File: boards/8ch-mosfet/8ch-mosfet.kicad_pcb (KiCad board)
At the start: 2 copper layers, 184.5 x 137 mm, 179 parts, among them J10 Screw_Terminal_01x02, J11 Screw_Terminal_01x02, J12 Screw_Terminal_01x02, J13 I2C, J14 N2K, J3 Screw_Terminal_01x08, J5 Screw_Terminal_01x02, J6 Screw_Terminal_01x02, J7 Screw_Terminal_01x02, J8 Screw_Terminal_01x02, J9 Screw_Terminal_01x02, M1 Fan_4pin, M2 Fan_4pin, Q1 2N7002, Q10 IRF4905, Q11 2N7002, Q12 IRF4905, Q13 2N7002, Q14 IRF4905, Q15 2N7002, Q16 IRF4905, Q2 IRF4905, Q3 2N7002, Q4 IRF4905, Q5 2N7002, Q6 IRF4905, Q7 2N7002, Q8 IRF4905, Q9 2N7002, U1 ESP32-DEVKITC, U10 ACS725xLCTR-20AU, U11 ACS725xLCTR-20AU, U12 ACS725xLCTR-20AU, U13 MCP1502-33, U15 MCP3425A0T-ECH, U2 MCP3208, U4 XL1509-5.0, U5 ACS725xLCTR-20AU, U6 ACS725xLCTR-20AU, U7 ACS725xLCTR-20AU, U8 ACS725xLCTR-20AU, U9 ACS725xLCTR-20AU

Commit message: updated BOM
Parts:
- F10: value mSMD100 -> mSMD110
- R10, R14, R18, R2, R22, R26, R30, R6: value 220 -> 220R

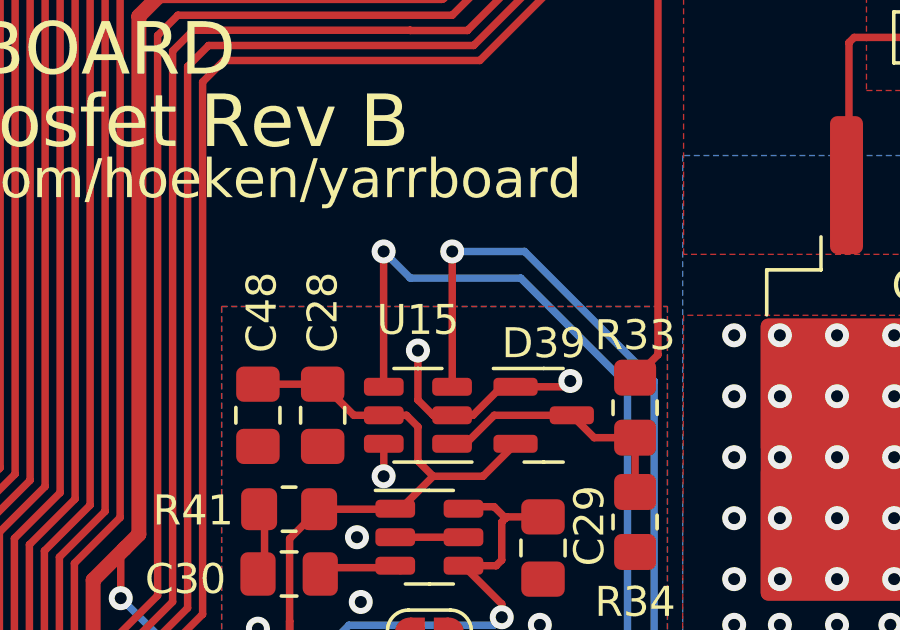
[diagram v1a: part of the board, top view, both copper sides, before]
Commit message: damnit, messed up the sda/scl lines on the board
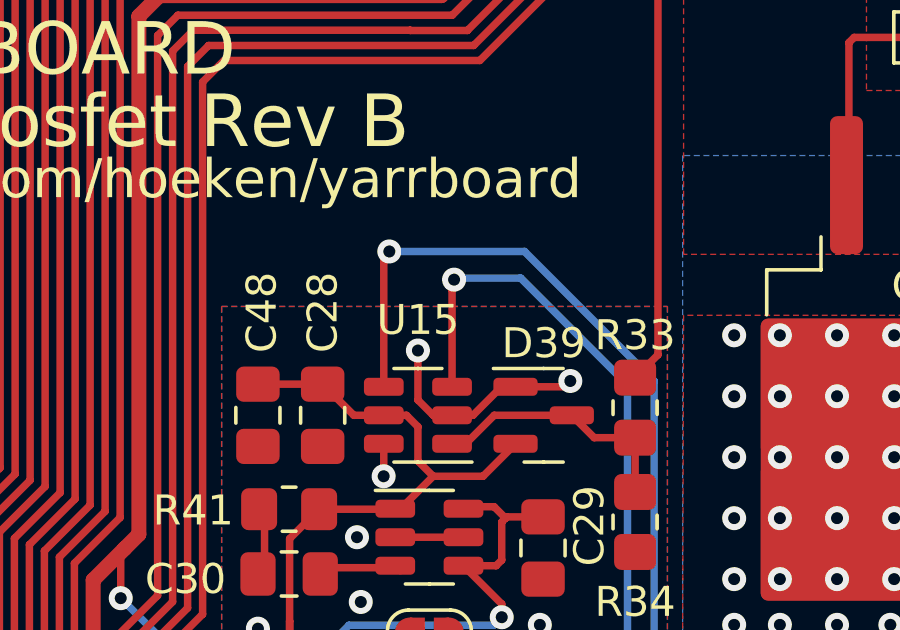
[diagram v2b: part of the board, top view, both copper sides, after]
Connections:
- U15 pad 3: SDA -> SCL
- U15 pad 4: SCL -> SDA
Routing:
- net SCL: track 85.2 -> 81.6 mm
- net SDA: track 88.8 -> 91.1 mm

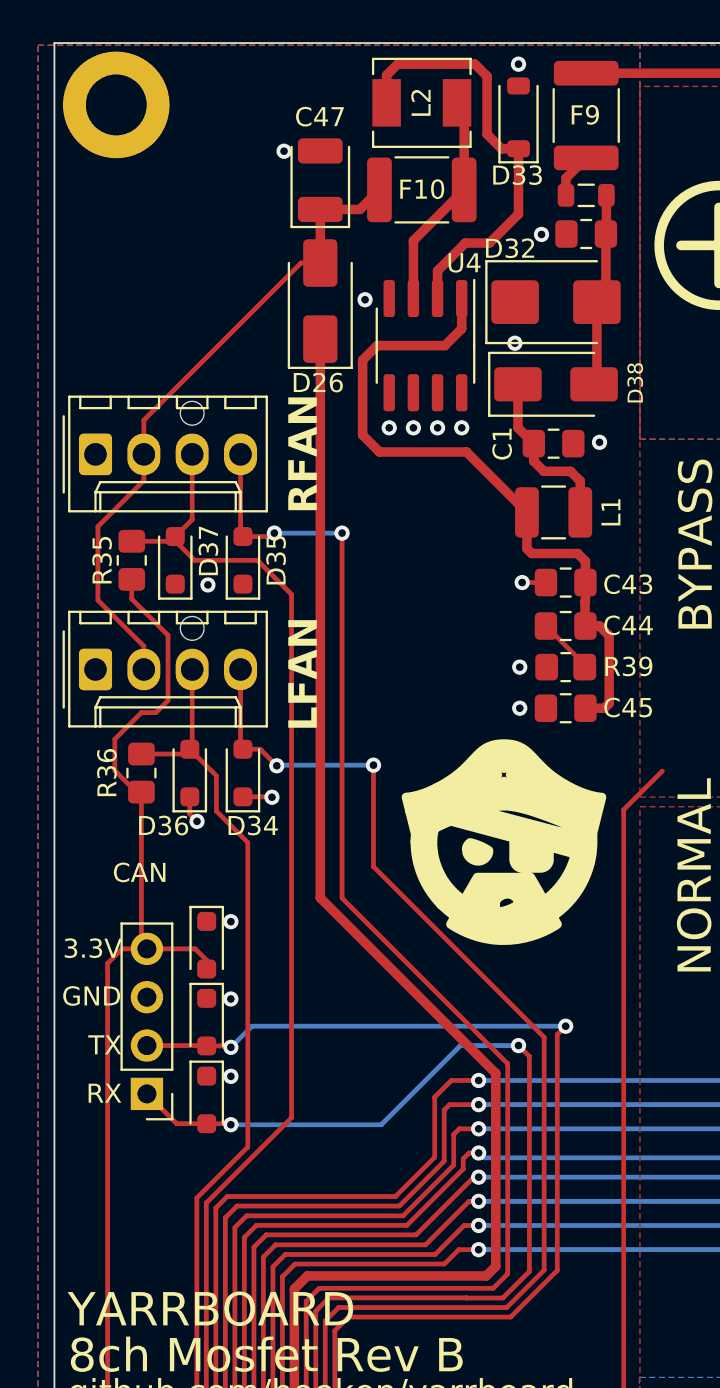
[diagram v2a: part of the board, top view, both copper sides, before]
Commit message: updated inductor footprint
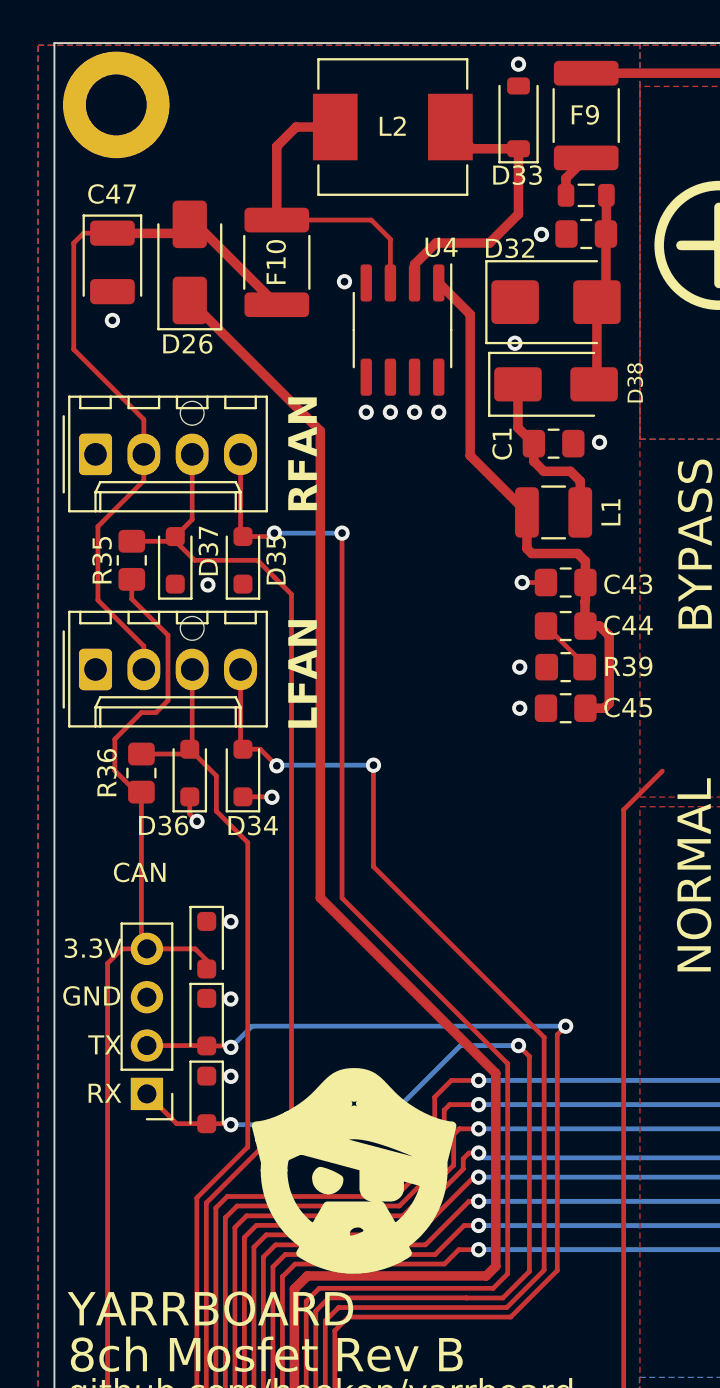
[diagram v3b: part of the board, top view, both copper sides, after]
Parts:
- L2: footprint Inductor_SMD:L_Chilisin_BMRA00040420 -> Inductor_SMD:L_Chilisin_BMRB00060650
- moved LOGO 19.0 mm to (65.7, 77.3)
- moved C47 11.7 mm to (53.0, 29.5), turned to -90 degrees
- moved F10 8.52 mm to (61.7, 29.5), turned to 90 degrees
- moved D26 7.15 mm to (57.1, 29.5)
- moved L2 1.98 mm to (67.8, 22.4), turned to 180 degrees
- moved U4 1.46 mm to (68.3, 33.1)
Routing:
- net Net-(U4-VIN): track 36.8 -> 29.0 mm
- net Net-(D33-K): track 22.6 -> 15.0 mm
- net ESP32_5V: track 162.8 -> 167.7 mm
- net +5V: track 34.1 -> 38.8 mm
- net Net-(U4-FB): track 11.5 -> 16.1 mm

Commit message: worked on the pwm issues
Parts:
- added C27: 100nF, Capacitor_SMD:C_0805_2012Metric_Pad1.18x1.45mm_HandSolder, F.Cu at (-61.8, 14.6)
- added C31: 1nF, Capacitor_SMD:C_0805_2012Metric_Pad1.18x1.45mm_HandSolder, F.Cu at (-61.8, 17.6)
- added C32: 4.7nF, Capacitor_SMD:C_0805_2012Metric_Pad1.18x1.45mm_HandSolder, F.Cu at (-61.8, 20.6)
- added C33: 100nF, Capacitor_SMD:C_0805_2012Metric_Pad1.18x1.45mm_HandSolder, F.Cu at (-55.5, 117.5)
- added C34: 1nF, Capacitor_SMD:C_0805_2012Metric_Pad1.18x1.45mm_HandSolder, F.Cu at (-55.5, 120.5)
- added C35: 4.7nF, Capacitor_SMD:C_0805_2012Metric_Pad1.18x1.45mm_HandSolder, F.Cu at (-55.5, 123.5)
- added C36: 1uF, Capacitor_SMD:C_0805_2012Metric_Pad1.18x1.45mm_HandSolder, F.Cu at (-55.5, 126.5)
- added D40: LED, LED_SMD:LED_0805_2012Metric_Pad1.15x1.40mm_HandSolder, F.Cu at (-50.7, 117.5)
- added D41: LED, LED_SMD:LED_0805_2012Metric_Pad1.15x1.40mm_HandSolder, F.Cu at (-63.2, 41.0)
- added D42: SS16, Diode_SMD:D_SMA, F.Cu at (-69.7, 41.8)
- added D43: SS16, Diode_SMD:D_SMA, F.Cu at (-53.8, 113.7)
- added F11: 25A, yarrboard:ATC Bypass Fuse, F.Cu at (-70.3, 35.2)
- added F12: 25A, yarrboard:ATC Bypass Fuse, F.Cu at (-63.9, 99.7)
- added J1: Screw_Terminal_01x02, yarrboard:Molex 1x02 .375, F.Cu at (-74.8, 21.9)
- added J2: Screw_Terminal_01x02, yarrboard:Molex 1x02 .375, F.Cu at (-68.4, 112.9)
- added Q17: IRFZ44, Package_TO_SOT_SMD:TO-252-2, F.Cu at (-85.5, 47.5)
- added Q18: IRFZ44, Package_TO_SOT_SMD:TO-252-2, F.Cu at (-72.0, 125.8)
- added R43: 0R, Resistor_SMD:R_0805_2012Metric_Pad1.20x1.40mm_HandSolder, F.Cu at (-50.6, 14.5)
- added R44: 56, Resistor_SMD:R_0805_2012Metric_Pad1.20x1.40mm_HandSolder, F.Cu at (-81.0, 56.5)
- added R46: 1k, Resistor_SMD:R_0805_2012Metric_Pad1.20x1.40mm_HandSolder, F.Cu at (-50.7, 120.5)
- added R47: 1k, Resistor_SMD:R_0805_2012Metric_Pad1.20x1.40mm_HandSolder, F.Cu at (-58.5, 41.0)
- added U14: ~, Package_SO:SO-4_4.4x4.3mm_P2.54mm, F.Cu at (-74.5, 49.5)
- added U16: ~, Package_SO:SOIC-8_3.9x4.9mm_P1.27mm, F.Cu at (-62.6, 125.0)
- added U17: ACS725xLCTR-20AU, yarrboard:ACS7XX, F.Cu at (-53.7, 107.7)
- added U3: ACS725xLCTR-20AU, yarrboard:ACS7XX, F.Cu at (-60.0, 25.8)
- C2: value 10nF/50v -> 10nF
- JP1: value SolderJumper_2_Open -> SolderJumper_3_Open; footprint Jumper:SolderJumper-2_P1.3mm_Open_RoundedPad1.0x1.5mm -> Jumper:SolderJumper-3_P1.3mm_Open_RoundedPad1.0x1.5mm_NumberLabels
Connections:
- C28 pad 1: REF_3V3 -> +3.3V
- C48 pad 1: REF_3V3 -> +3.3V
- C49 pad 1: REF_3V3 -> Net-(JP1-C)
- D39 pad 2: REF_3V3 -> +3.3V
- JP1 pad 1: REF_3V3 -> +3.3V
- JP1 pad 2: +3.3V -> Net-(JP1-C)
- U1 pad 5: FAN_TACH2 -> unconnected-(U1-GPIO34-Pad5)
- U15 pad 5: REF_3V3 -> +3.3V
- U2 pad 15: REF_3V3 -> Net-(JP1-C)

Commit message: starting a redesign ahead of having parts to test. wish me luck
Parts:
- removed C27, C33: 100nF, Capacitor_SMD:C_0805_2012Metric_Pad1.18x1.45mm_HandSolder
- removed C31, C34: 1nF, Capacitor_SMD:C_0805_2012Metric_Pad1.18x1.45mm_HandSolder
- removed C32, C35: 4.7nF, Capacitor_SMD:C_0805_2012Metric_Pad1.18x1.45mm_HandSolder
- removed C36: 1uF, Capacitor_SMD:C_0805_2012Metric_Pad1.18x1.45mm_HandSolder
- removed D18, D19, D20, D21, D22, D23, D24, D25: 15V, Diode_SMD:D_SOD-323_HandSoldering
- removed D40, D41: LED, LED_SMD:LED_0805_2012Metric_Pad1.15x1.40mm_HandSolder
- removed D42, D43: SS16, Diode_SMD:D_SMA
- removed F11, F12: 25A, yarrboard:ATC Bypass Fuse
- removed J1, J2: Screw_Terminal_01x02, yarrboard:Molex 1x02 .375
- removed Q1, Q11, Q13, Q15, Q3, Q5, Q7, Q9: 2N7002, Package_TO_SOT_SMD:SOT-23
- removed Q17, Q18: IRFZ44, Package_TO_SOT_SMD:TO-252-2
- removed R23, R27, R31: 100K, Resistor_SMD:R_0805_2012Metric_Pad1.20x1.40mm_HandSolder
- removed R24, R28, R32: 22K, Resistor_SMD:R_0805_2012Metric_Pad1.20x1.40mm_HandSolder
- removed R26, R30: 220R, Resistor_SMD:R_0805_2012Metric_Pad1.20x1.40mm_HandSolder
- removed R44: 56, Resistor_SMD:R_0805_2012Metric_Pad1.20x1.40mm_HandSolder
- removed R46, R47: 1k, Resistor_SMD:R_0805_2012Metric_Pad1.20x1.40mm_HandSolder
- removed U14: ~, Package_SO:SO-4_4.4x4.3mm_P2.54mm
- removed U16: ~, Package_SO:SOIC-8_3.9x4.9mm_P1.27mm
- removed U17, U3: ACS725xLCTR-20AU, yarrboard:ACS7XX
- added C37: 1uF, Capacitor_SMD:C_0805_2012Metric_Pad1.18x1.45mm_HandSolder, F.Cu at (-32.2, 22.9)
- added C38: 1uF, Capacitor_SMD:C_0805_2012Metric_Pad1.18x1.45mm_HandSolder, F.Cu at (-20.6, 51.6)
- added C39: 1uF, Capacitor_SMD:C_0805_2012Metric_Pad1.18x1.45mm_HandSolder, F.Cu at (-20.6, 22.9)
- added C40: 1uF, Capacitor_SMD:C_0805_2012Metric_Pad1.18x1.45mm_HandSolder, F.Cu at (-32.2, 51.6)
- added C41: 1uF, Capacitor_SMD:C_0805_2012Metric_Pad1.18x1.45mm_HandSolder, F.Cu at (-20.6, 37.3)
- added C42: 1uF, Capacitor_SMD:C_0805_2012Metric_Pad1.18x1.45mm_HandSolder, F.Cu at (-9.05, 22.9)
- added C46: 1uF, Capacitor_SMD:C_0805_2012Metric_Pad1.18x1.45mm_HandSolder, F.Cu at (-32.2, 37.3)
- added C50: 1uF, Capacitor_SMD:C_0805_2012Metric_Pad1.18x1.45mm_HandSolder, F.Cu at (-9.05, 37.3)
- added U18: ~, Package_SO:SOIC-8_3.9x4.9mm_P1.27mm, F.Cu at (-35.1, 18.2)
- added U19: ~, Package_SO:SOIC-8_3.9x4.9mm_P1.27mm, F.Cu at (-23.5, 46.9)
- added U20: ~, Package_SO:SOIC-8_3.9x4.9mm_P1.27mm, F.Cu at (-23.5, 18.2)
- added U21: ~, Package_SO:SOIC-8_3.9x4.9mm_P1.27mm, F.Cu at (-35.1, 46.9)
- added U22: ~, Package_SO:SOIC-8_3.9x4.9mm_P1.27mm, F.Cu at (-23.5, 32.5)
- added U23: ~, Package_SO:SOIC-8_3.9x4.9mm_P1.27mm, F.Cu at (-12.0, 18.2)
- added U24: ~, Package_SO:SOIC-8_3.9x4.9mm_P1.27mm, F.Cu at (-35.1, 32.5)
- added U25: ~, Package_SO:SOIC-8_3.9x4.9mm_P1.27mm, F.Cu at (-12.0, 32.5)
- Q10, Q12, Q14, Q16, Q2, Q4, Q6, Q8: value IRF4905 -> IRFR7446; footprint Package_TO_SOT_SMD:TO-263-2 -> Package_TO_SOT_SMD:TO-252-2
- R10, R14, R18, R2, R22, R6: value 220R -> 0
- R11, R15, R19, R3, R7: value 100K -> 0
- R12, R16, R20, R4, R8: value 22K -> 0
- moved R20 206.9 mm to (-37.0, 40.2)
- moved R22 201.1 mm to (-13.8, 40.2)
- moved R18 193.7 mm to (-25.4, 40.2)
- moved R19 188.5 mm to (-13.8, 25.8), turned to 0 degrees
- moved R16 185.7 mm to (-37.0, 54.5)
- moved R15 181.3 mm to (-25.4, 25.8), turned to 0 degrees
- moved R12 173.5 mm to (-37.0, 25.8)
- moved R14 173.0 mm to (-25.4, 54.5)
- moved R10 168.1 mm to (-37.0, 37.2)
- moved R11 148.7 mm to (-13.8, 37.2), turned to 0 degrees
- moved R6 146.9 mm to (-37.0, 51.6)
- moved R7 141.5 mm to (-25.4, 37.2), turned to 0 degrees
- moved R8 135.3 mm to (-13.8, 22.9)
- moved R2 135.1 mm to (-37.0, 22.9)
- moved R4 128.5 mm to (-25.4, 22.9)
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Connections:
- F1 pad 1: Net-(D18-K) -> Net-(Q2-D)
- F1 pad 3: Net-(Q2-D) -> Net-(Q2-S)
- F2 pad 1: Net-(D19-K) -> Net-(Q4-D)
- F2 pad 3: Net-(Q4-D) -> Net-(Q4-S)
- F3 pad 1: Net-(D20-K) -> Net-(Q6-D)
- F3 pad 3: Net-(Q6-D) -> Net-(Q6-S)
- F4 pad 1: Net-(D21-K) -> Net-(Q8-D)
- F4 pad 3: Net-(Q8-D) -> Net-(Q8-S)
- F5 pad 1: Net-(D22-K) -> Net-(Q10-D)
- F5 pad 3: Net-(Q10-D) -> Net-(Q10-S)
- F6 pad 1: Net-(D23-K) -> Net-(Q12-D)
- F6 pad 3: Net-(Q12-D) -> Net-(Q12-S)
- F7 pad 1: Net-(D24-K) -> Net-(Q14-D)
- F7 pad 3: Net-(Q14-D) -> Net-(Q14-S)
- F8 pad 1: Net-(D25-K) -> Net-(Q16-D)
- F8 pad 3: Net-(Q16-D) -> Net-(Q16-S)
- Q10 pad 1: Net-(D22-A) -> Net-(Q10-G)
- Q10 pad 3: Net-(D22-K) -> Net-(Q10-S)
- Q12 pad 1: Net-(D23-A) -> Net-(Q12-G)
- Q12 pad 3: Net-(D23-K) -> Net-(Q12-S)
- Q14 pad 1: Net-(D24-A) -> Net-(Q14-G)
- Q14 pad 3: Net-(D24-K) -> Net-(Q14-S)
- Q16 pad 1: Net-(D25-A) -> Net-(Q16-G)
- Q16 pad 3: Net-(D25-K) -> Net-(Q16-S)
- Q2 pad 1: Net-(D18-A) -> Net-(Q2-G)
- Q2 pad 3: Net-(D18-K) -> Net-(Q2-S)
- Q4 pad 1: Net-(D19-A) -> Net-(Q4-G)
- Q4 pad 3: Net-(D19-K) -> Net-(Q4-S)
- Q6 pad 1: Net-(D20-A) -> Net-(Q6-G)
- Q6 pad 3: Net-(D20-K) -> Net-(Q6-S)
- Q8 pad 1: Net-(D21-A) -> Net-(Q8-G)
- Q8 pad 3: Net-(D21-K) -> Net-(Q8-S)
- R10 pad 1: /CHANNEL 2/PWM -> Net-(Q14-G)
- R11 pad 1: Net-(D20-A) -> Net-(Q16-G)
- R11 pad 2: Net-(D20-K) -> Net-(R11-Pad2)
- R12 pad 1: Net-(Q5-D) -> Net-(Q2-G)
- R12 pad 2: Net-(D20-A) -> Net-(R12-Pad2)
- R14 pad 1: /CHANNEL 3/PWM -> Net-(Q4-G)
- R15 pad 1: Net-(D21-A) -> Net-(Q6-G)
- R15 pad 2: Net-(D21-K) -> Net-(R15-Pad2)
- R16 pad 1: Net-(Q7-D) -> Net-(Q8-G)
- R16 pad 2: Net-(D21-A) -> Net-(R16-Pad2)
- R18 pad 1: /CHANNEL 4/PWM -> Net-(Q10-G)
- R19 pad 1: Net-(D22-A) -> Net-(Q12-G)
- R19 pad 2: Net-(D22-K) -> Net-(R19-Pad2)
- R2 pad 1: /CHANNEL 0/PWM -> Net-(Q2-G)
- R20 pad 1: Net-(Q9-D) -> Net-(Q14-G)
- R20 pad 2: Net-(D22-A) -> Net-(R20-Pad2)
- R22 pad 1: /CHANNEL 5/PWM -> Net-(Q16-G)
- R3 pad 1: Net-(D18-A) -> Net-(Q4-G)
- R3 pad 2: Net-(D18-K) -> Net-(R3-Pad2)
- R4 pad 1: Net-(Q1-D) -> Net-(Q6-G)
- R4 pad 2: Net-(D18-A) -> Net-(R4-Pad2)
- R6 pad 1: /CHANNEL 1/PWM -> Net-(Q8-G)
- R7 pad 1: Net-(D19-A) -> Net-(Q10-G)
- R7 pad 2: Net-(D19-K) -> Net-(R7-Pad2)
- R8 pad 1: Net-(Q3-D) -> Net-(Q12-G)
- R8 pad 2: Net-(D19-A) -> Net-(R8-Pad2)
- U10 pad 1: Net-(Q12-D) -> Net-(Q12-S)
- U10 pad 2: Net-(Q12-D) -> Net-(Q12-S)
- U11 pad 1: Net-(Q14-D) -> Net-(Q14-S)
- U11 pad 2: Net-(Q14-D) -> Net-(Q14-S)
- U12 pad 1: Net-(Q16-D) -> Net-(Q16-S)
- U12 pad 2: Net-(Q16-D) -> Net-(Q16-S)
- U5 pad 1: Net-(Q2-D) -> Net-(Q2-S)
- U5 pad 2: Net-(Q2-D) -> Net-(Q2-S)
- U6 pad 1: Net-(Q4-D) -> Net-(Q4-S)
- U6 pad 2: Net-(Q4-D) -> Net-(Q4-S)
- U7 pad 1: Net-(Q6-D) -> Net-(Q6-S)
- U7 pad 2: Net-(Q6-D) -> Net-(Q6-S)
- U8 pad 1: Net-(Q8-D) -> Net-(Q8-S)
- U8 pad 2: Net-(Q8-D) -> Net-(Q8-S)
- U9 pad 1: Net-(Q10-D) -> Net-(Q10-S)
- U9 pad 2: Net-(Q10-D) -> Net-(Q10-S)
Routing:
- net (no net): track 0.00 -> 154.7 mm
- net Net-(R6-Pad2): track 9.64 -> 0.00 mm
- net Net-(R22-Pad2): track 9.64 -> 0.00 mm
- net Net-(Q15-G): track 9.64 -> 0.00 mm
- net Net-(Q13-G): track 9.64 -> 0.00 mm
- net Net-(R2-Pad2): track 9.64 -> 0.00 mm
- net Net-(R18-Pad2): track 9.64 -> 0.00 mm
- net Net-(R14-Pad2): track 9.64 -> 0.00 mm
- net Net-(R10-Pad2): track 9.64 -> 0.00 mm
- net Net-(D25-A): track 9.59 -> 0.00 mm
- net Net-(D24-A): track 9.59 -> 0.00 mm
- net Net-(D23-A): track 9.59 -> 0.00 mm
- net Net-(D19-A): track 9.59 -> 0.00 mm
- net Net-(D18-A): track 9.59 -> 0.00 mm
- net Net-(D22-A): track 9.59 -> 0.00 mm
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- added copper zone on F.Cu, net Net-(Q2-S)
- removed copper zone on F.Cu, net Net-(D18-K)
- removed copper zone on F.Cu, net Net-(D19-K)
- removed copper zone on F.Cu, net Net-(D20-K)
- removed copper zone on F.Cu, net Net-(D21-K)
- removed copper zone on F.Cu, net Net-(D22-K)
- removed copper zone on F.Cu, net Net-(D23-K)
- removed copper zone on F.Cu, net Net-(D24-K)
- removed copper zone on F.Cu, net Net-(D25-K)
